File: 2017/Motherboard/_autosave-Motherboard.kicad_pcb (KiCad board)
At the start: 2 copper layers, 47 parts, among them P1 DB9, P2 PROGRAM+DEBUG, P3 PCIe Card 1, P4 PCIe Card 2, P5 PCIe Card 3, SW1 SPST, U1 MSP432, U2 LM340MP-5.0, U3 LD1086DT33TR, U4 MCP9808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

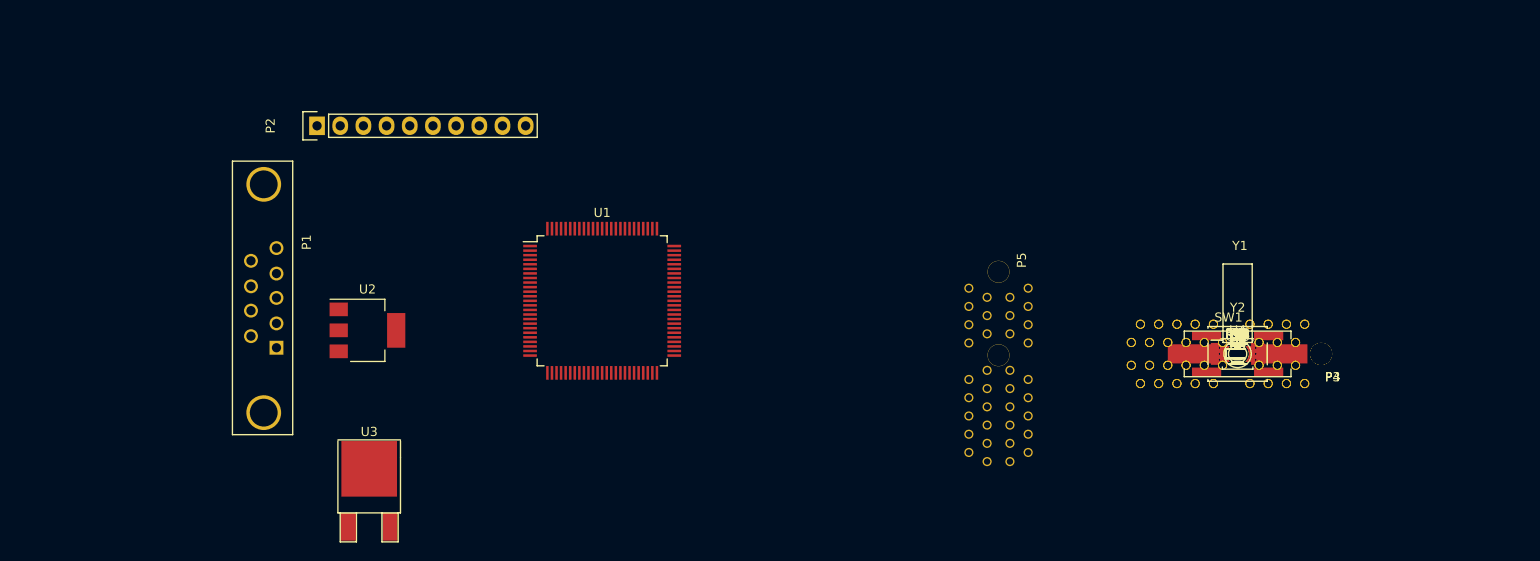
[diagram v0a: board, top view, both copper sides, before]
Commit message: Start layout of motherboard
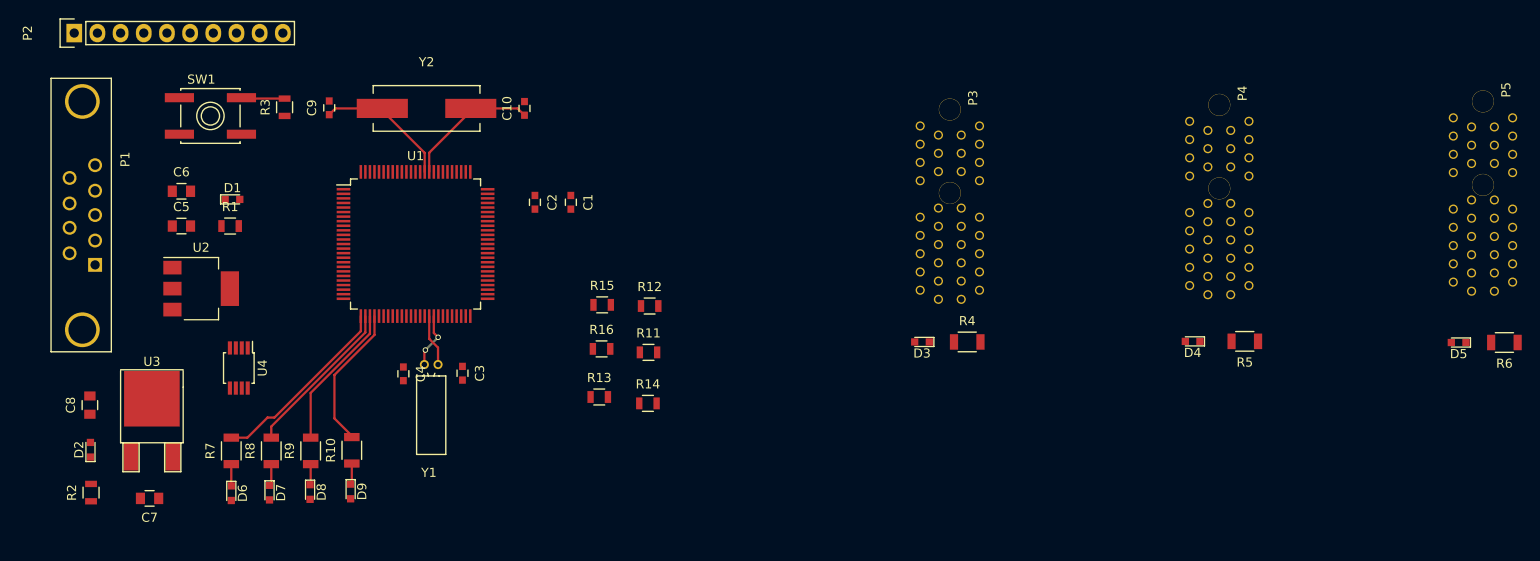
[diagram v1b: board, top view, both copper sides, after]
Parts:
- moved R2 126.6 mm to (22.9, 120.2), turned to 90 degrees
- moved D2 126.1 mm to (22.8, 115.5), turned to 90 degrees
- moved C8 125.9 mm to (22.7, 110.6), turned to 90 degrees
- moved C7 120.3 mm to (29.3, 120.8), turned to 180 degrees
- moved C6 117.1 mm to (32.8, 87.2)
- moved C5 116.6 mm to (32.8, 91.0)
- moved SW1 115.5 mm to (35.9, 78.9)
- moved D1 111.4 mm to (38.4, 88.1)
- moved D6 111.3 mm to (38.2, 120.3), turned to 270 degrees
- moved R1 111.3 mm to (38.1, 91.0)
- moved R7 110.8 mm to (38.2, 115.6), turned to 90 degrees
- moved U4 109.5 mm to (39.1, 106.6), turned to 270 degrees
- moved R3 107.9 mm to (44.1, 78.0), turned to 90 degrees
- moved D7 107.2 mm to (42.4, 120.2), turned to 270 degrees
- moved R8 106.4 mm to (42.6, 115.6), turned to 90 degrees
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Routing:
- net /TestLED1: track 0.00 -> 20.7 mm
- net /TestLED2: track 0.00 -> 17.6 mm
- net /TestLED3: track 0.00 -> 16.0 mm
- net /TestLED4: track 0.00 -> 15.9 mm
- net /HFXOUT: track 0.00 -> 15.0 mm
- net /HFXIN: track 0.00 -> 15.0 mm
- net /LFXOUT: track 0.00 -> 6.13 mm, vias 0 -> 2
- net /LFXIN: track 0.00 -> 5.71 mm
- net /RSTn: track 0.00 -> 4.77 mm
- net Net-(D7-Pad1): track 0.00 -> 2.40 mm
- net Net-(D6-Pad1): track 0.00 -> 2.39 mm
- net Net-(D9-Pad1): track 0.00 -> 2.31 mm
- net Net-(D8-Pad1): track 0.00 -> 2.28 mm
